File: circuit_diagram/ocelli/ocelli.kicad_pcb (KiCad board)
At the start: 2 copper layers, 89.9 x 58.8 mm, 119 parts, among them J1 Conn_01x06, J2 Conn_01x06, J3 Conn_01x06, J4 Conn_01x06, J5 Conn_01x08, J6 Conn_01x02, J7 Conn_01x02, Q1 BSS138, Q10 BSS138, Q2 ST-1KL3A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

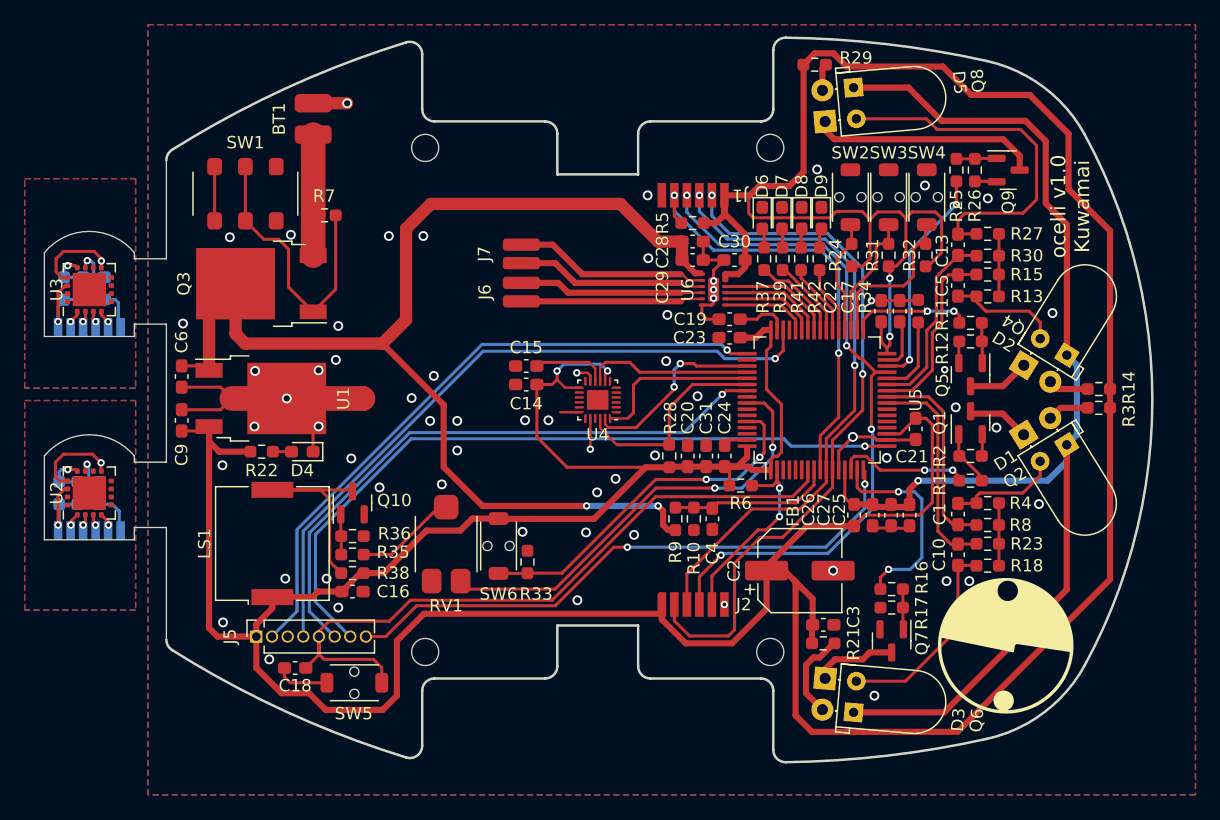
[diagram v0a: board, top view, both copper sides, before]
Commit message: バッテリコネクタ変更
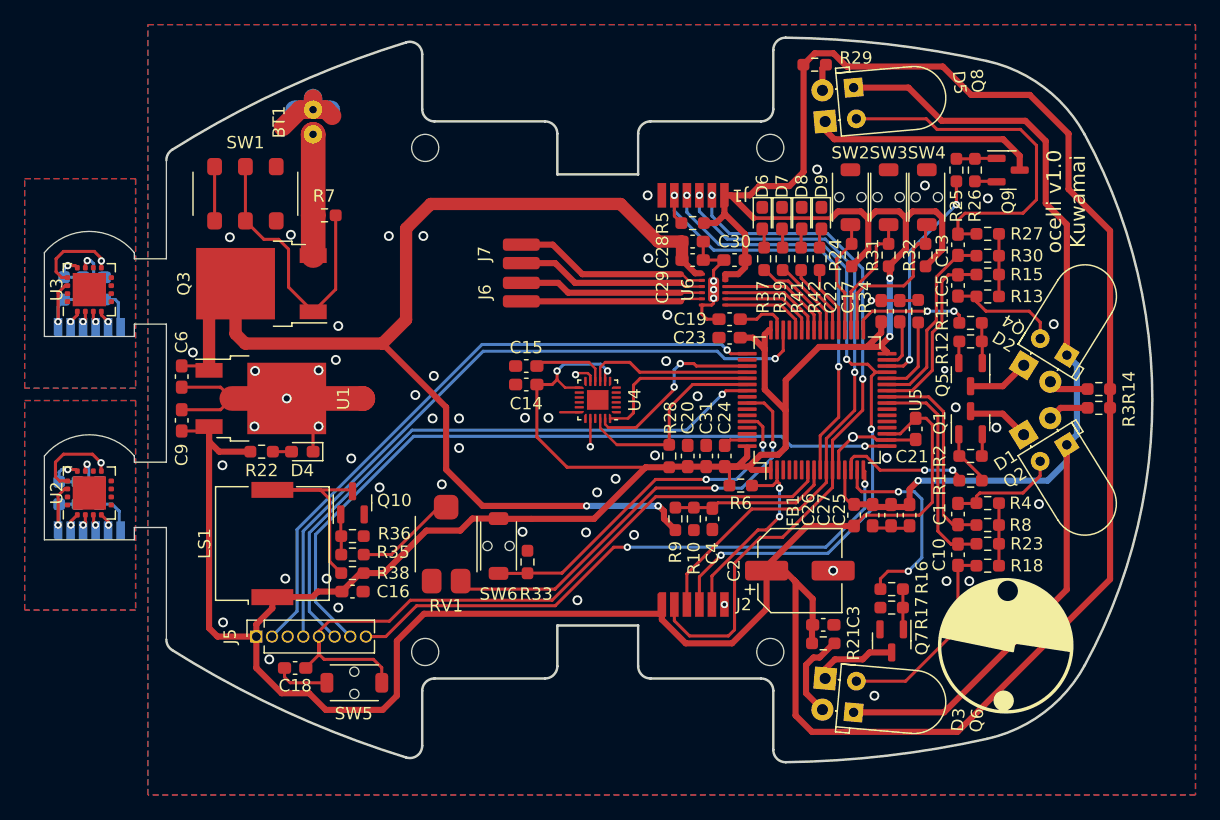
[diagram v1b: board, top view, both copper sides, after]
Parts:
- moved BT1 0.25 mm to (120.9, 77.9)
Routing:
- net +3.3V: track 392.9 -> 402.5 mm
- net GND: track 77.7 -> 84.4 mm, vias 62 -> 61
- net SPI2_SCLK: track 56.5 -> 57.2 mm
